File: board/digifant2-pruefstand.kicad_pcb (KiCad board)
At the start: 2 copper layers, 144 x 114 mm, 62 parts, among them J0 VW ECU HARNESS, J1 12V BENCH IN, J2 IDLE VALVE N71, J3 OLED / UI I2C, Q1 2N7002, Q2 P-MOS -30V >=5A, Q3 2N7002, Q4 2N7002, Q5 2N7002, SW1 PUSH, SW2 PUSH, SW3 PUSH, U1 INA226 (0x40), U2 MCP4728 (0x60), U3 INA226 (0x41), U4 AD9833, U5 Raspberry Pi Pico, U6 TS5A3159A, U7 TS5A3159A, U8 TS5A3159A, Y1 25MHz

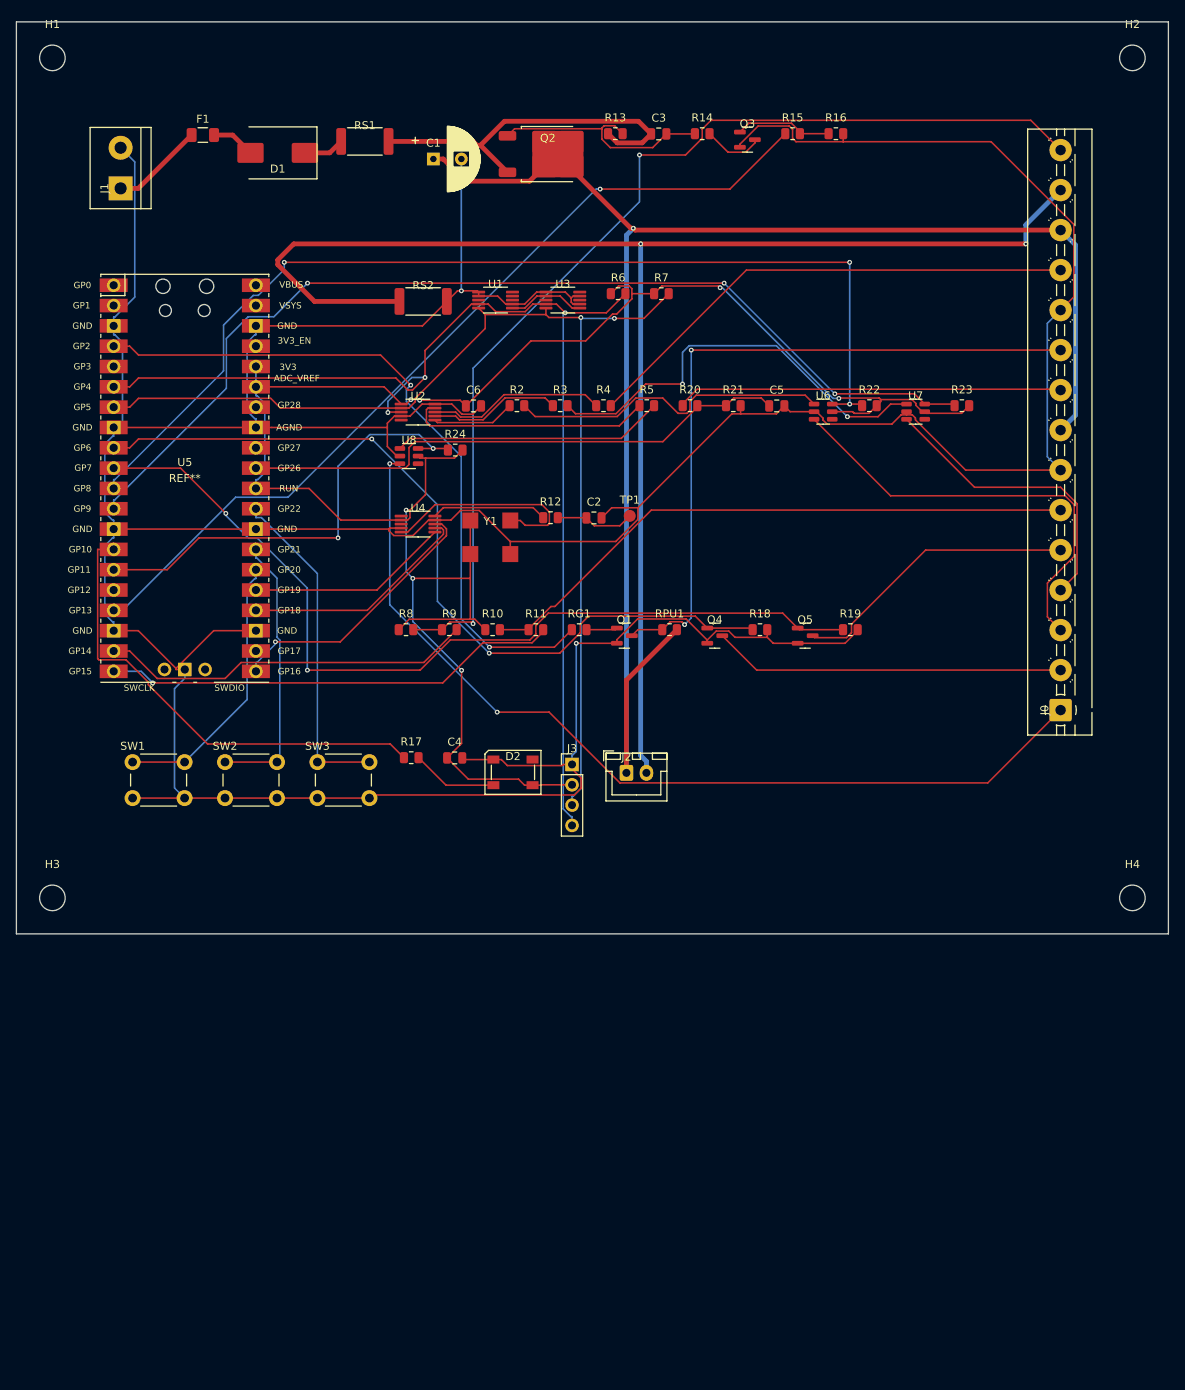
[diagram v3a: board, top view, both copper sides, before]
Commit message: Fix throttle-switch model + give the OLED header real clearance
Corrections sourced from the user's own hands-on Digifant HiL notes:
- VW-6 is sensor/idle-switch common ground, not a 2nd switch contact -- wired
  to GND directly. Only one idle switch, on VW-11 (Q5). Removed Q4/R18/GP7.
- VW-18 confirmed for the crank/Hall signal (needs >=8-10V amplitude per the
  user's own bench notes), resolving the earlier VW-8-vs-18 ambiguity.
- R10 1k injector pull-up validated (their bench found 10k too weak, even
  2.2k marginal).
- Noted VW-3 fuel-pump-relay monitoring and per-signal indicator LEDs as
  possible future additions, per the user's original HiL design.

Also: J3 (OLED header) now gets its own ~40mm clear band at the bottom of the
board, isolated from D2/J2 which used to sit only ~7mm away -- a 0.96" OLED
module plugged in flat would have overhung them. Board grew to 144x154mm.

Co-Authored-By: Claude Sonnet 5 <noreply@anthropic.com>
Claude-Session: https://claude.ai/code/session_01XcEuUwwCT37oProAm8HYeY
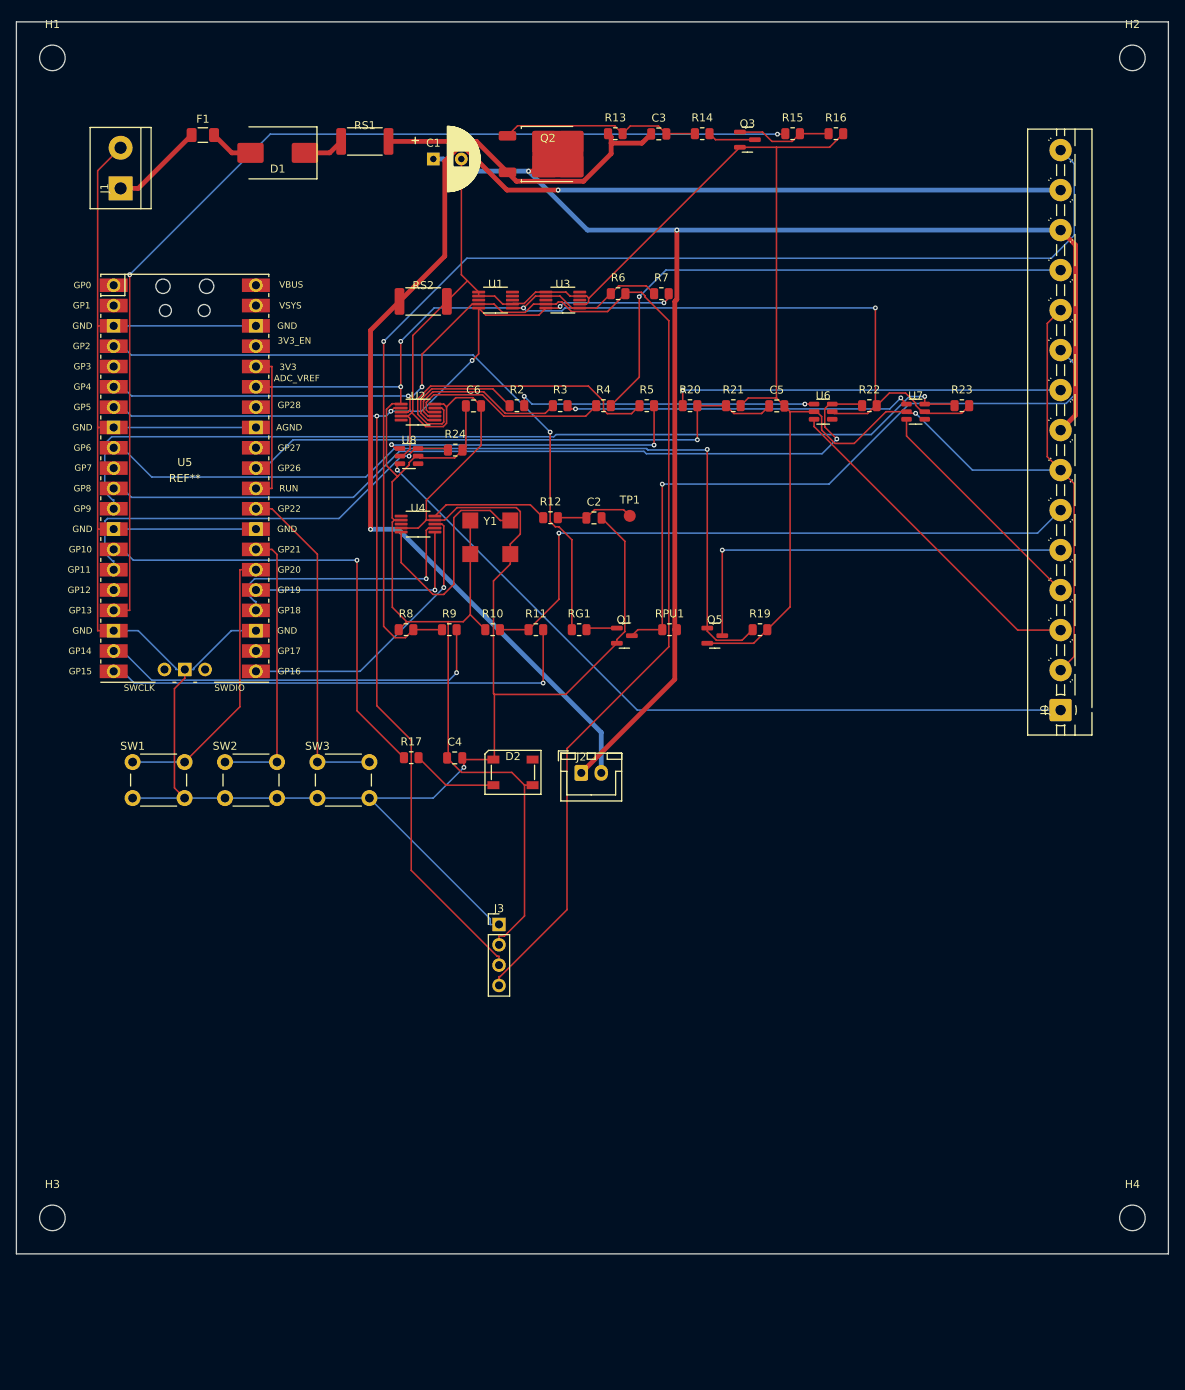
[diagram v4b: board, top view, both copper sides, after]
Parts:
- removed Q4: 2N7002, Package_TO_SOT_SMD:SOT-23
- removed R18: 100k, Resistor_SMD:R_0805_2012Metric
- moved H3 40.0 mm to (4.50, 149.5)
- moved H4 40.0 mm to (139.5, 149.5)
- moved J3 22.0 mm to (60.3, 112.8)
- moved R19 11.3 mm to (92.9, 76.0)
- moved Q5 11.3 mm to (87.3, 76.7)
- moved J2 5.65 mm to (70.6, 93.9)
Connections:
- J0 pad 2: VW_PIN6 -> GND
- Q5 pad 1: GP7_THROTTLE_WOT_SW -> GP6_THROTTLE_IDLE_SW
- R19 pad 1: GP7_THROTTLE_WOT_SW -> GP6_THROTTLE_IDLE_SW
- U5 pad 10: GP7_THROTTLE_WOT_SW -> unconnected-(U5-Pad10-Pad10)
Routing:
- net GP7_THROTTLE_WOT_SW: track 112.2 -> 0.00 mm, vias 2 -> 0
- net VW_PIN6: track 44.1 -> 0.00 mm
- net I2C_SDA: track 147.4 -> 176.0 mm, vias 3 -> 2
- net GP8_AIRTEMP_CONNECT: track 129.8 -> 103.5 mm, vias 3 -> 1
- net GP13_ECU_PWR_EN: track 108.6 -> 133.2 mm, vias 1 -> 2
- net +3V3: track 260.1 -> 283.0 mm, vias 7 -> 4
- net GND: track 592.3 -> 614.3 mm
- net VW_PIN2: track 115.8 -> 96.3 mm, vias 2 -> 1
- net VW_PIN11: track 36.2 -> 53.0 mm, vias 0 -> 1
- net I2C_SCL: track 141.3 -> 157.1 mm, vias 2 -> 5
- net VW_PIN25: track 131.8 -> 147.1 mm, vias 2 -> 1
- net VW_PIN23_VALVE_RETURN: track 187.0 -> 174.0 mm
- net VW_PIN9: track 54.7 -> 42.3 mm
- net +12V_ECU_SW: track 205.7 -> 194.0 mm, vias 1 -> 2
- net R3_SW_IN: track 53.0 -> 43.5 mm
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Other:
- board size 144 x 114 mm -> 144 x 154 mm

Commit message: Give the Pico's USB port real clearance from J1
J1 (12V screw terminal) was only ~7.5mm from U5's USB end, X-overlapping it --
a plugged-in cable would likely have fouled the terminal block / its wires.
Moved U5 down (gap now 23mm); cascaded Row A and the OLED zone down to match,
board grew to 144x169mm.

Co-Authored-By: Claude Sonnet 5 <noreply@anthropic.com>
Claude-Session: https://claude.ai/code/session_01XcEuUwwCT37oProAm8HYeY
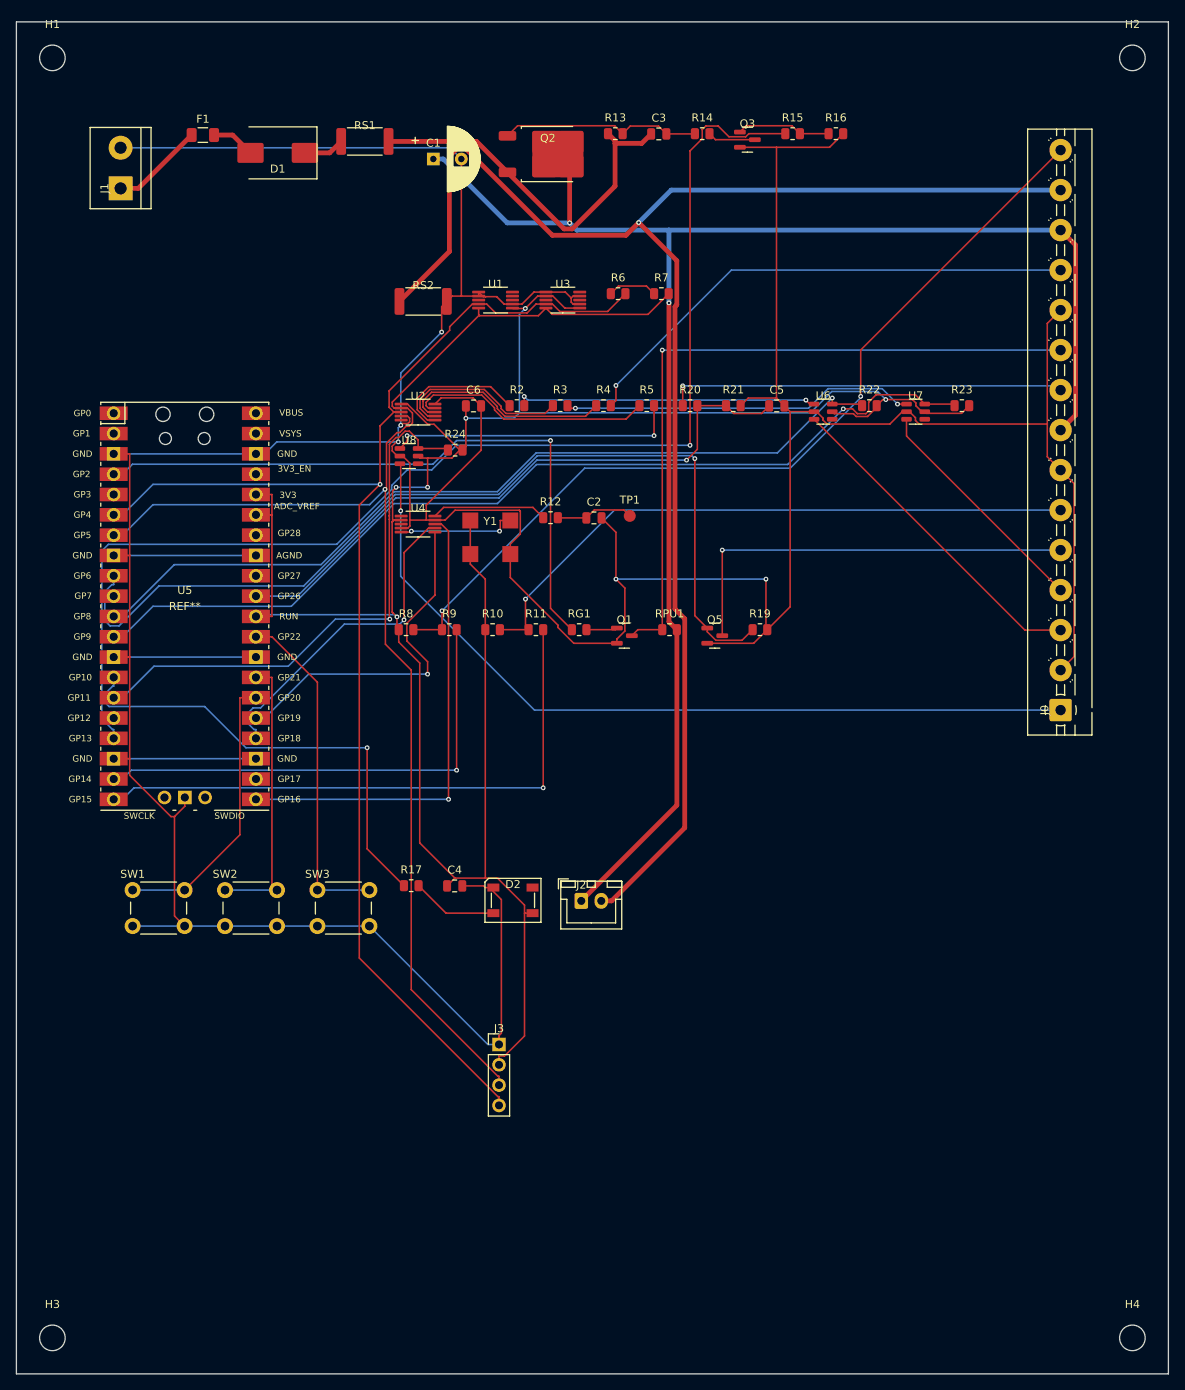
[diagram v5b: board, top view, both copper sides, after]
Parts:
- moved C4 16.0 mm to (54.8, 108.0)
- moved D2 16.0 mm to (62.1, 109.8)
- moved J2 16.0 mm to (70.6, 109.9)
- moved R17 16.0 mm to (49.4, 108.0)
- moved SW1 16.0 mm to (14.5, 108.5)
- moved SW2 16.0 mm to (26.1, 108.5)
- moved SW3 16.0 mm to (37.6, 108.5)
- moved U5 16.0 mm to (21.1, 73.0)
- moved H3 15.0 mm to (4.50, 164.5)
- moved H4 15.0 mm to (139.5, 164.5)
- moved J3 15.0 mm to (60.3, 127.8)
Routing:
- net VW_PIN25: track 147.1 -> 110.6 mm, vias 1 -> 2
- net GP16_SPI_CS: track 36.7 -> 59.7 mm
- net VW_PIN23_VALVE_RETURN: track 174.0 -> 196.8 mm, vias 2 -> 1
- net GP13_ECU_PWR_EN: track 133.2 -> 154.8 mm, vias 2 -> 1
- net +3V3: track 283.0 -> 304.5 mm, vias 4 -> 6
- net +12V_ECU_SW: track 194.0 -> 215.1 mm
- net GND: track 614.3 -> 633.6 mm, vias 2 -> 5
- net GP11_LAMBDA_CONNECT: track 53.5 -> 70.1 mm
- net I2C_SCL: track 157.1 -> 173.5 mm, vias 5 -> 1
- net GP19_SPI_MOSI: track 29.6 -> 44.0 mm
- net N$3: track 28.9 -> 15.0 mm, vias 0 -> 2
- net GP15_INJ_CAPTURE: track 61.0 -> 74.1 mm
- net GP6_THROTTLE_IDLE_SW: track 106.7 -> 118.1 mm
- net GP14_IGN_CAPTURE: track 50.1 -> 60.9 mm
- net R5_DAC_SIDE: track 39.3 -> 30.8 mm
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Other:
- board size 144 x 154 mm -> 144 x 169 mm

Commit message: Move J2 (idle valve) next to RS2/U3 to shorten its traces
Was ~75mm away in the button row; now sits right next to the current-sense
components it electrically belongs with.

Co-Authored-By: Claude Sonnet 5 <noreply@anthropic.com>
Claude-Session: https://claude.ai/code/session_01XcEuUwwCT37oProAm8HYeY
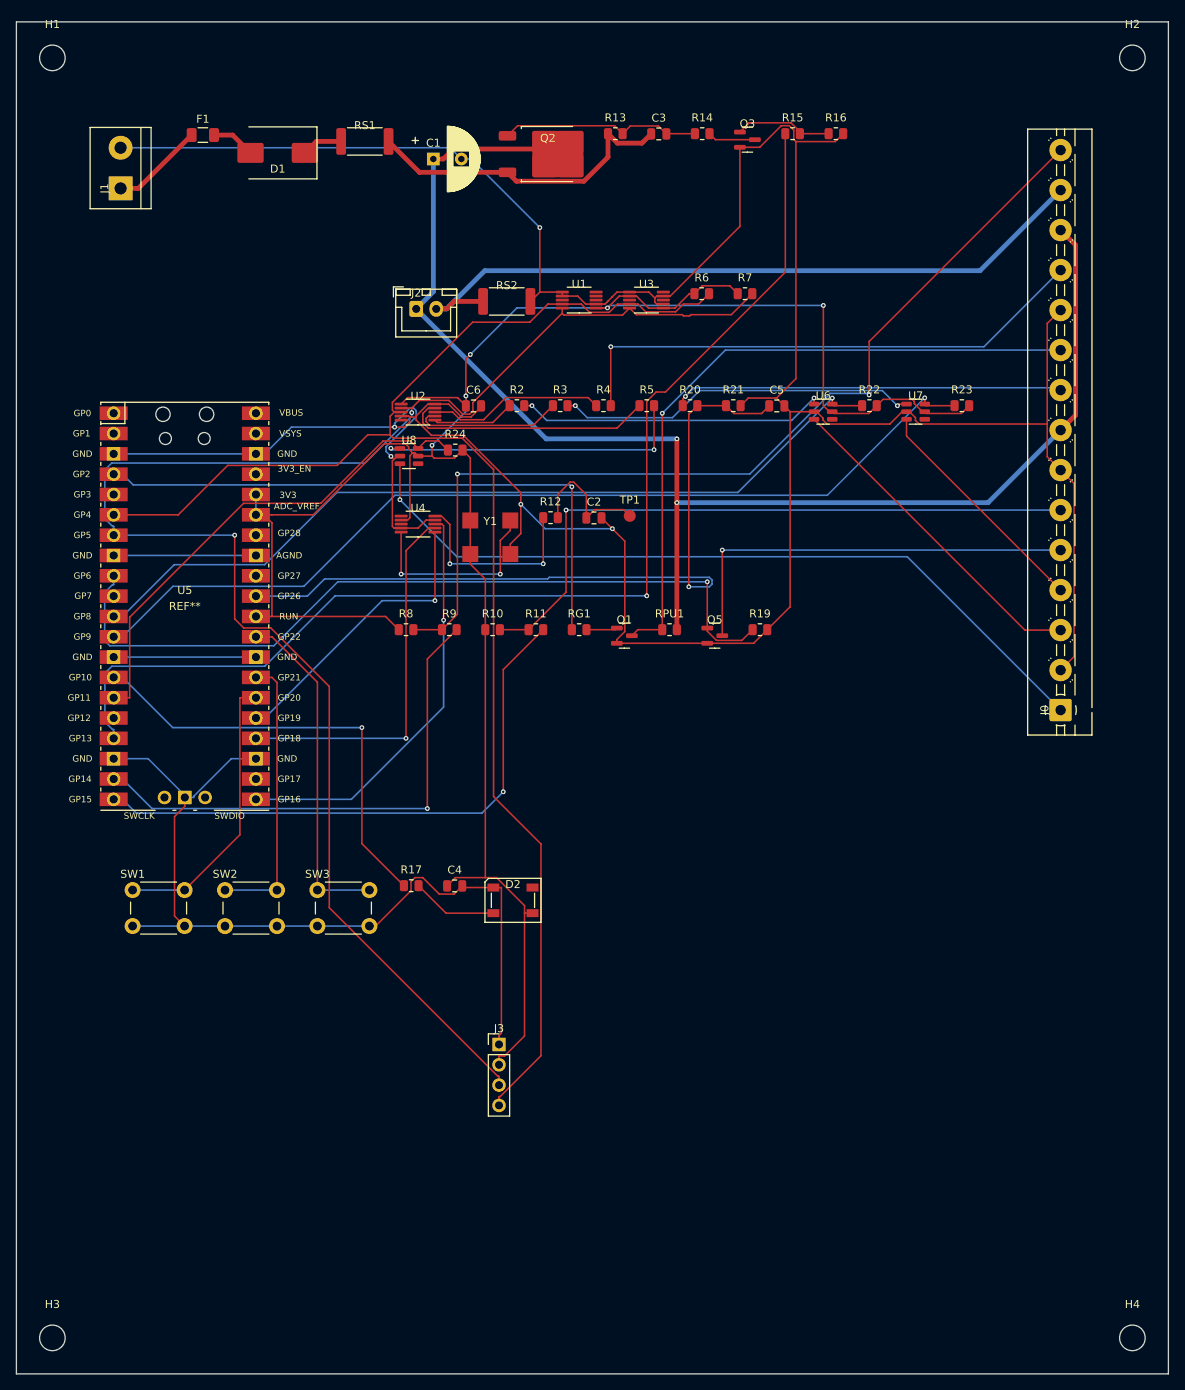
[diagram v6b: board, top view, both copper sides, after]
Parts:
- moved J2 76.8 mm to (50.0, 35.9)
- moved R6 10.5 mm to (85.7, 34.0)
- moved R7 10.5 mm to (91.1, 34.0)
- moved RS2 10.5 mm to (61.3, 34.9)
- moved U1 10.4 mm to (70.3, 34.8)
- moved U3 10.4 mm to (78.8, 34.8)
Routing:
- net VW_PIN23_VALVE_RETURN: track 196.8 -> 90.4 mm, vias 1 -> 0
- net GND: track 633.6 -> 574.2 mm
- net I2C_SCL: track 173.5 -> 204.0 mm, vias 1 -> 2
- net +12V_ECU_SW: track 215.1 -> 185.6 mm
- net I2C_SDA: track 171.0 -> 189.7 mm, vias 1 -> 0
- net GP6_THROTTLE_IDLE_SW: track 118.1 -> 100.4 mm
- net GP26_AFM_REF_ADC: track 78.0 -> 94.5 mm
- net +3V3: track 304.5 -> 288.4 mm, vias 6 -> 5
- net U4_VOUT_R: track 14.5 -> 24.6 mm, vias 0 -> 2
- net N$3: track 15.0 -> 24.9 mm
- net VW_PIN25: track 110.6 -> 120.1 mm
- net GP13_ECU_PWR_EN: track 154.8 -> 146.1 mm
- net GP11_LAMBDA_CONNECT: track 70.1 -> 62.2 mm, vias 1 -> 0
- net GP16_SPI_CS: track 59.7 -> 52.1 mm
- net U4_LOAD: track 9.72 -> 16.8 mm
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
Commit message: Layout surgery: real netclasses, GND reconnected, Kelvin taps, direct 12V rail
Per a deep layout review (Opus), fixed the issues that mattered electrically:

- Real 'Power' (0.8mm) / 'Gnd' (0.5mm) KiCad netclasses -- previously the
  0.6mm widths only existed inside the Freerouting session file, so any
  hand-routed trace (including these Kelvin taps) would have defaulted to
  0.2mm with no DRC check to catch it.
- GND was split into 4 disconnected islands (the whole operator-UI cluster --
  buttons, LED, OLED header -- had no copper ground return at all) and
  physically routed the ECU's full return current through U1/U3's own
  ground pads. Ripped up the ad-hoc daisy chain and let it re-route as one
  connected net with the new Gnd class.
- U1/U3 now get dedicated, short Kelvin sense traces to RS1/RS2 instead of
  being unrouted (U1) or sharing 18.7mm of the general GND chain (U3, ~83mV
  of error on a 60mV full-scale signal).
- +12V_ECU_SW no longer detours 135mm through J2 with two extra vias --
  re-routed directly from Q2's tab, ~65mm point-to-point.

Ground pour and D1/Q2 thermal copper were attempted (fix_layout.py history)
but scripted zone placement kept landing disconnected from or shorting into
other nets in this dense a board -- left as a to-do for the KiCad GUI where
the overlap can be seen. A handful of DRC items remain right at the tight
U1/U3/RS1/RS2 cluster for the same reason (manual nudge, like the historical
INA226-fanout items).

fix_layout.py / reroute_missing.py are the reproducible tools for this pass.

Co-Authored-By: Claude Sonnet 5 <noreply@anthropic.com>
Claude-Session: https://claude.ai/code/session_01XcEuUwwCT37oProAm8HYeY
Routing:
- net +12V_POST_D1: track 5.12 -> 42.4 mm
- net +12V_ECU: track 40.0 -> 72.8 mm
- net VW_PIN23_VALVE_RETURN: track 90.4 -> 113.0 mm
- net GND: track 574.2 -> 590.8 mm
